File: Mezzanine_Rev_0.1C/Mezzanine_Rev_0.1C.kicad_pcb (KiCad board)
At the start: 2 copper layers, 170 x 85.1 mm, 62 parts, among them J1 QBUS_DWK_64Pin_MBT, J2 DIP20 Header, J3 DIP20 Header, J4 IDC-64M, J5 IDC-16M, J6 IDC-20M, J7 Conn_01x03_Pin, J8 PLD-16R, U1 1533LI1, U10 74LS07, U11 74LS74, U2 1533TM2, U3 1533LA8, U4 CD74HCT4067M, U5 1533LE4, U6 1533AP6, U7 1533AP6, U8 74LS07, U9 74LS07

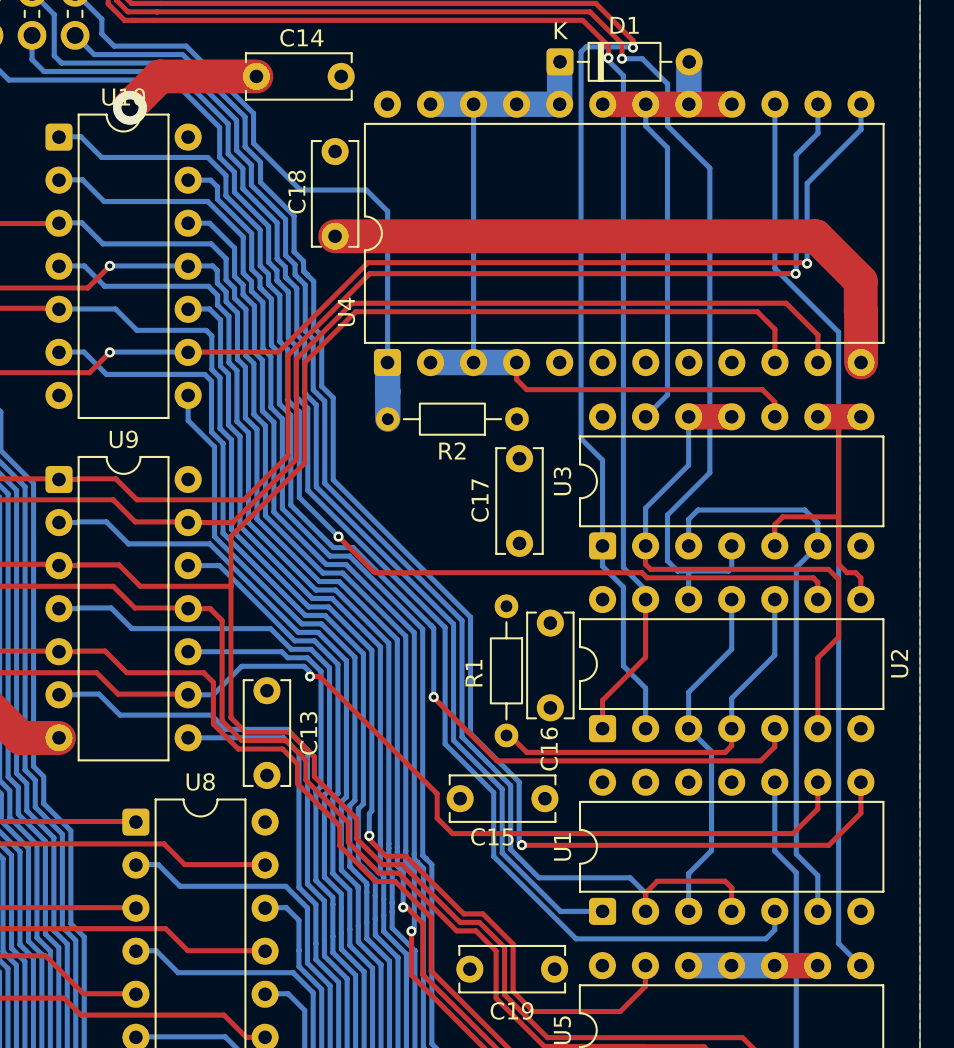
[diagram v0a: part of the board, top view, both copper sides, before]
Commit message: Mezzanine: SOIC option for U4
DIP version is rare, let's give another option.
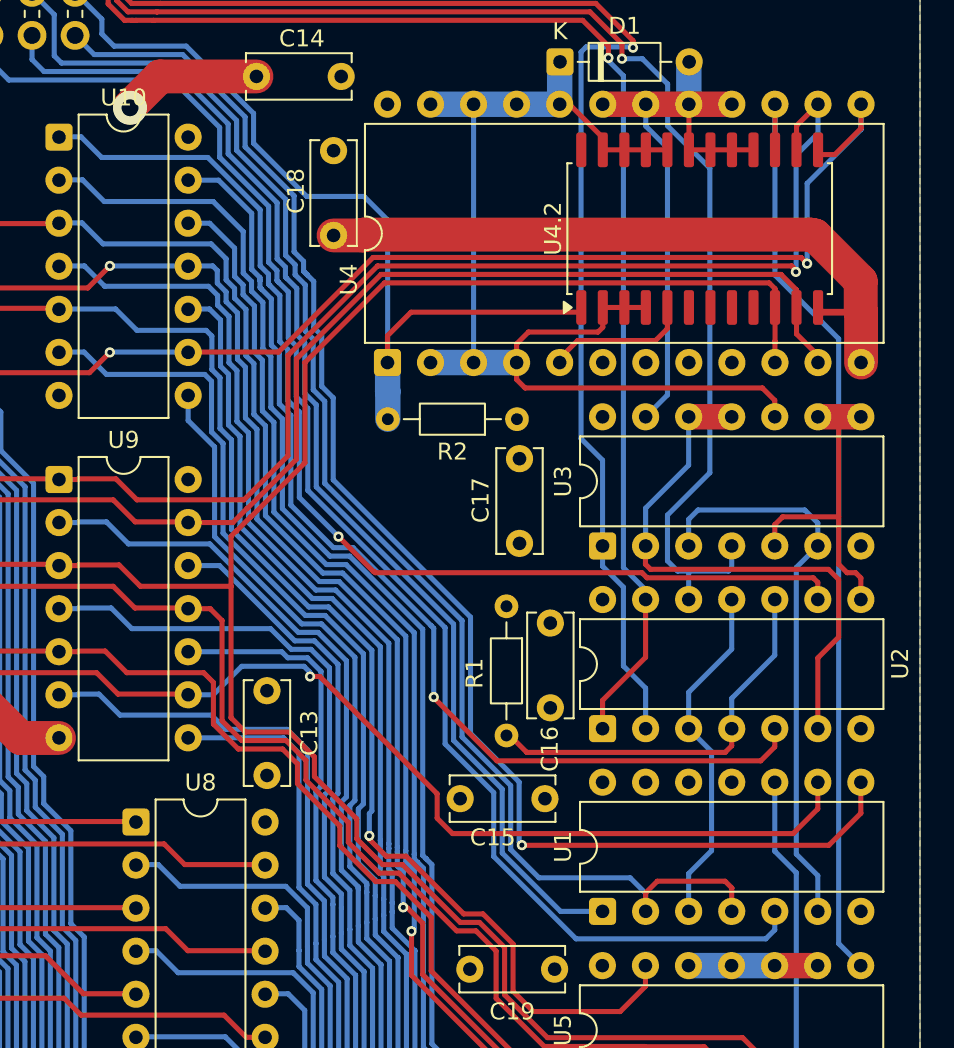
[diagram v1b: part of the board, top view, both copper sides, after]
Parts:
- added U4.2: CD74HCT4067M, Package_SO:SOIC-24W_7.5x15.4mm_P1.27mm, F.Cu at (206.4, 62.3)
- moved C18 0.10 mm to (184.8, 57.7)
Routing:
- net Net-(D1-K): track 48.1 -> 65.0 mm
- net ~{LOCK}: track 37.6 -> 50.9 mm
- net GND: track 243.2 -> 254.2 mm
- net Net-(D1-A): track 29.6 -> 36.1 mm
- net /~{A12}: track 132.8 -> 137.7 mm
- net /~{A11}: track 139.2 -> 142.7 mm
- net /~{A9}: track 188.5 -> 191.3 mm
- net Net-(U4-~{E}): track 52.9 -> 55.6 mm
- net /~{A10}: track 134.7 -> 136.6 mm

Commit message: Mezzanine: Proper types for U4
Distinguish DIP vs SOIC
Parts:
- U4: value CD74HCT4067M -> CD4067BE
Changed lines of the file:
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@@
 			)
 		)
-		(property "Value" "CD74HCT4067M"
+		(property "Value" "CD4067BE"
 			(at 7.62 30.27 90)
 			(layer "F.Fab")
